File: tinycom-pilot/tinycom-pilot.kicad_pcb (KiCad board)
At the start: 2 copper layers, 45.2 x 45.2 mm, 34 parts, among them J1 MICRO_SD_HINGE, P1 CONN_02X08, P2 CONN_02X08, P3 USB_A, U1 SY8008BAAC, U2 SY8008BAAC, U3 SY8008BAAC, U4 conn-3x10, U5 STM32-48PIN, U6 MPU6050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

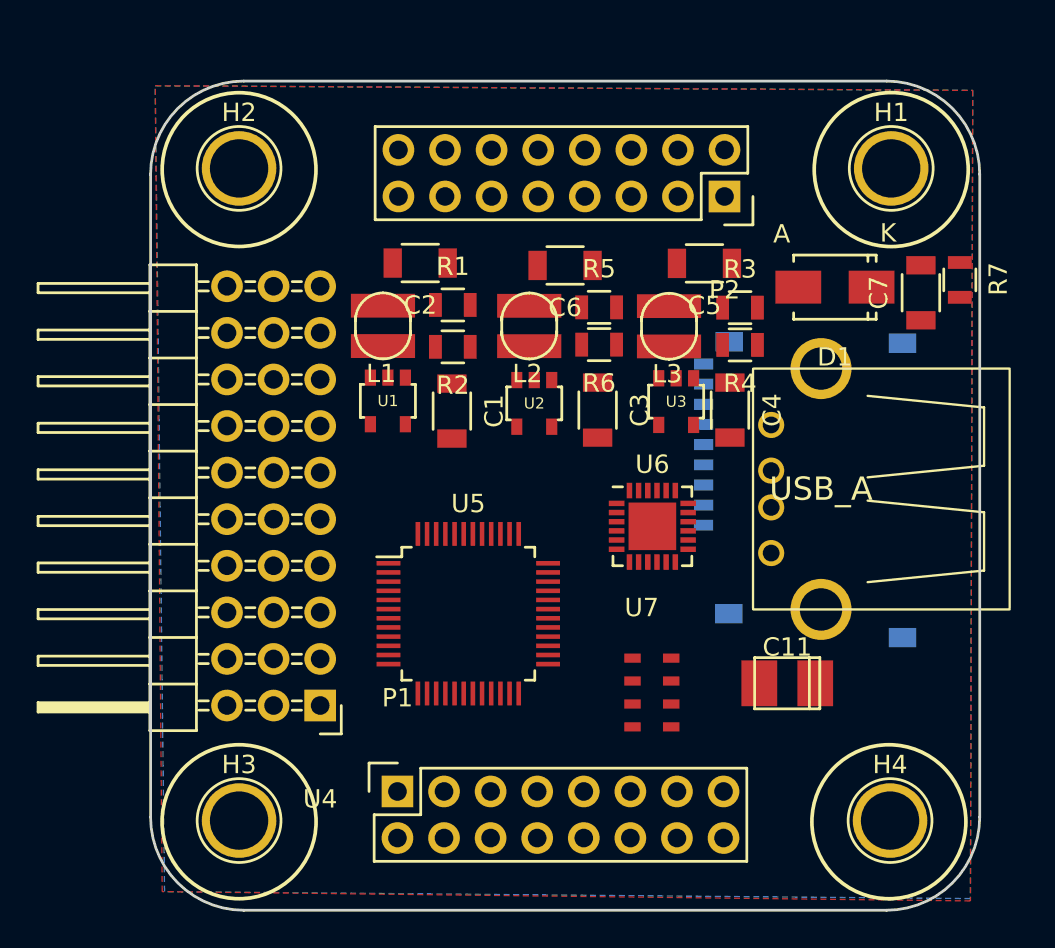
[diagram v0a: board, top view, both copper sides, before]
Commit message: change connectors
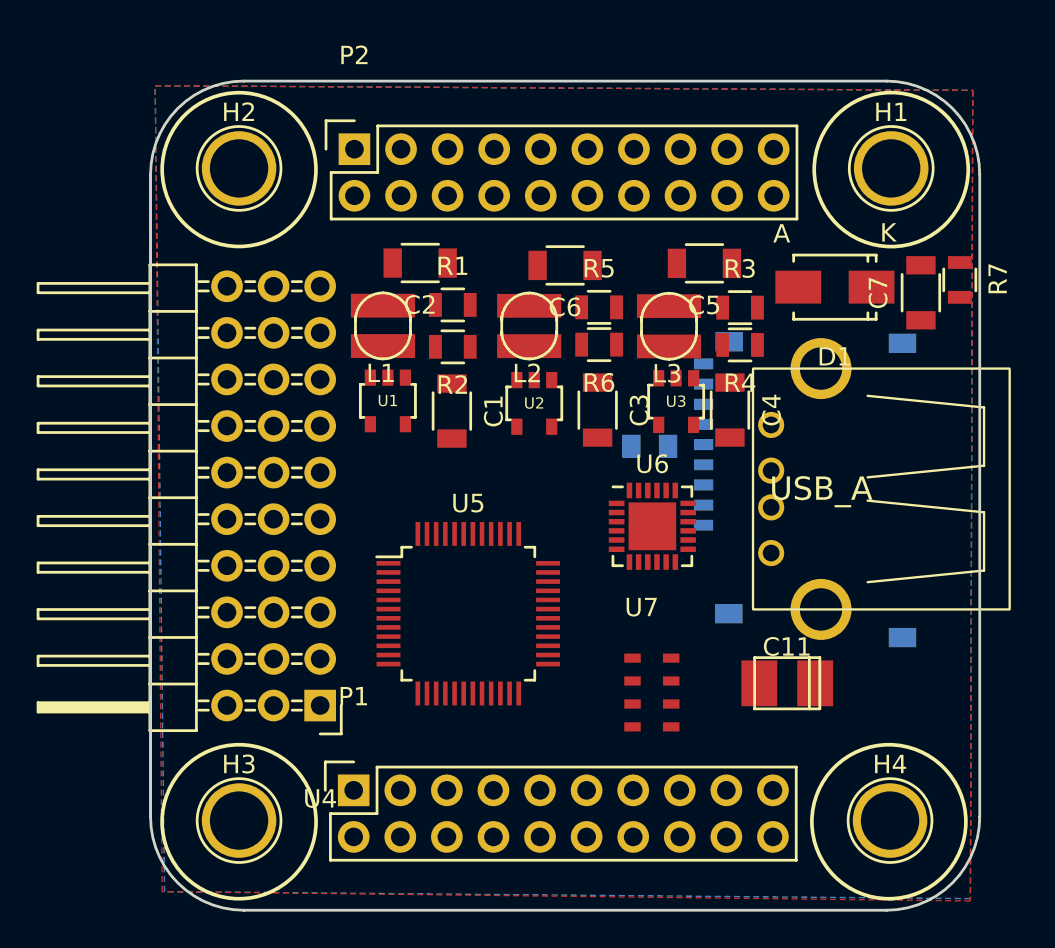
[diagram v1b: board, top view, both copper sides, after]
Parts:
- added C8: C_Small, Capacitors_SMD:C_0805, B.Cu at (151.7, 99.2)
- P1, P2: value CONN_02X08 -> CONN_02X10; footprint Socket_Strips:Socket_Strip_Straight_2x08 -> Socket_Strips:Socket_Strip_Straight_2x10
- moved P2 20.3 mm to (135.6, 83.0), turned to 0 degrees
- moved P1 2.39 mm to (135.5, 117.9)
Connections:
- J1 pad 1: SDC0_D2 -> (no net)
- J1 pad 2: SDC0_D3 -> (no net)
- J1 pad 3: SDC0_CMD -> (no net)
- J1 pad 5: SDC0_CLK -> (no net)
- J1 pad 7: SDC0_D0 -> (no net)
- J1 pad 8: SDC0_D1 -> (no net)
- P1 pad 10: UDP1 -> (no net)
- P1 pad 11: SDC0_CMD -> (no net)
- P1 pad 12: UDM1 -> (no net)
- P1 pad 13: SDC0_D3 -> (no net)
- P1 pad 15: SDC0_D2 -> (no net)
- P1 pad 2: GND -> (no net)
- P1 pad 4: VCC_15 -> (no net)
- P1 pad 5: SDC0_D1 -> (no net)
- P1 pad 6: VCC_14 -> (no net)
- P1 pad 7: SDC0_D0 -> (no net)
- P1 pad 8: VCC_33 -> (no net)
- P1 pad 9: SDC0_CLK -> (no net)
- P2 pad 2: GND -> (no net)
- P2 pad 4: VCC_30 -> (no net)
- P3 pad 2: UDM1 -> (no net)
- P3 pad 3: UDP1 -> (no net)
